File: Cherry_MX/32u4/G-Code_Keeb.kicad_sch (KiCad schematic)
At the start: 45 parts, among them J1 Conn_01x04, SW1 SW_Push_45deg, SW10 SW_Push_45deg, SW11 SW_Push_45deg, SW12 SW_Push_45deg, SW13 SW_Push_45deg, SW14 SW_Push_45deg, SW15 SW_Push_45deg, SW16 SW_Push_45deg, SW17 SW_Push_45deg, SW18 SW_Push_45deg, SW19 SW_Push_45deg, SW2 SW_Push_45deg, SW20 SW_Push_45deg, SW21 SW_Push_45deg, SW22 SW_Push_45deg, SW23 SW_Push_45deg, SW24 SW_Push, SW25 SW_Push, SW3 SW_Push_45deg, SW4 SW_Push_45deg, SW5 SW_Push_45deg, SW6 SW_Push_45deg, SW7 SW_Push_45deg, SW8 SW_Push_45deg, SW9 SW_Push_45deg, U1 ATmega32U4-A, Y1 16MHz

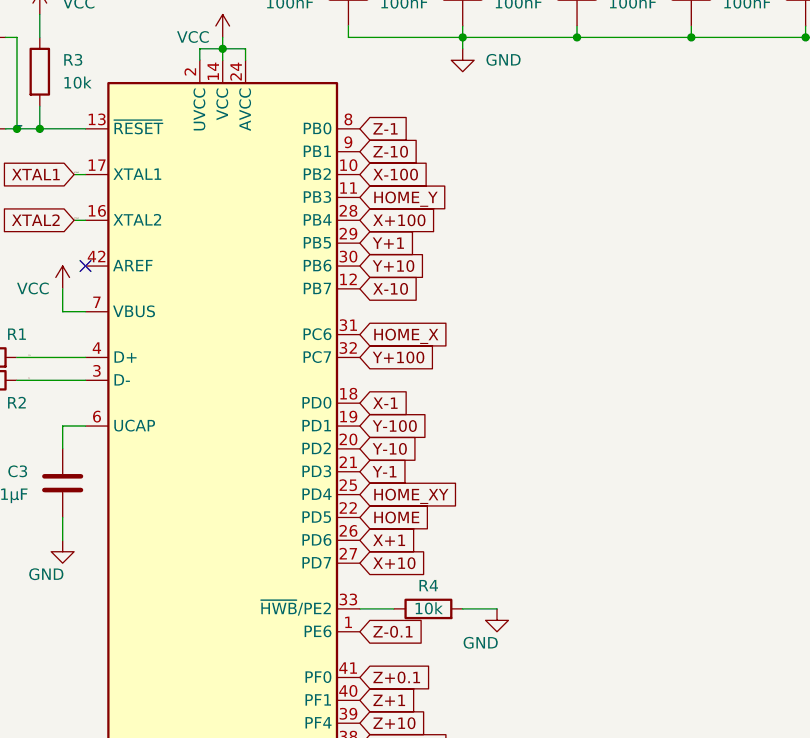
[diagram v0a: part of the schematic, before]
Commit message: Fixed mistake on X axis
The X axis values were mirrored, this commit fix that. That also includes the silkscreen.
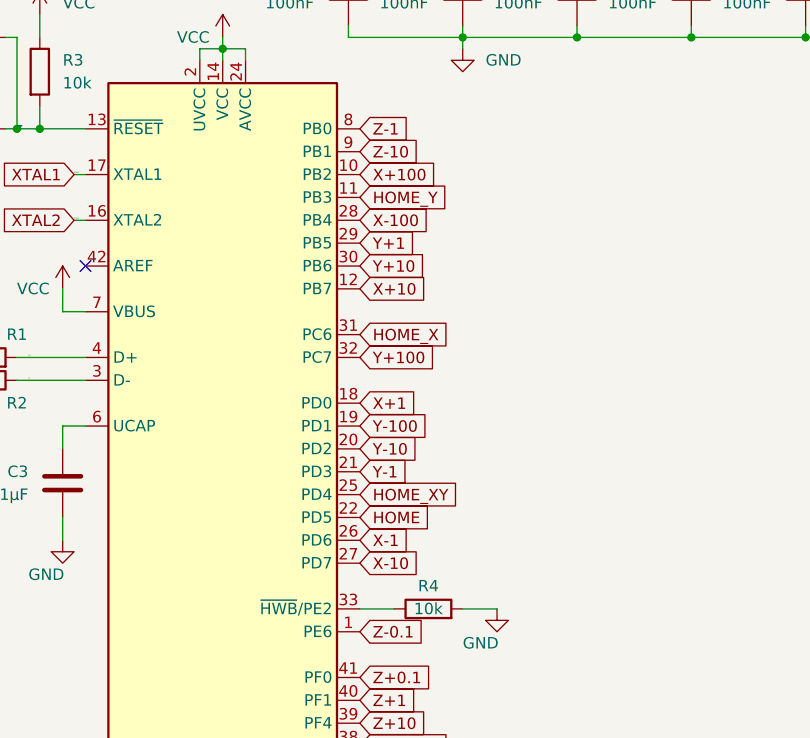
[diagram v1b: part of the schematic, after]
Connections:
- net X+1: now also U1.18 (PD0); no longer U1.26 (PD6)
- net X+10: now also U1.12 (PB7); no longer U1.27 (PD7)
- net X+100: now also U1.10 (PB2); no longer U1.28 (PB4)
- net X-1: now also U1.26 (PD6); no longer U1.18 (PD0)
- net X-10: now also U1.27 (PD7); no longer U1.12 (PB7)
- net X-100: now also U1.28 (PB4); no longer U1.10 (PB2)
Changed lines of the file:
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@@
     )
   )
-  (global_label "X-1" (shape input) (at 218.44 72.39 0) (fields_autoplaced)
-    (effects (font (size 1.27 1.27)) (justify left))
-    (property "Intersheet References" "${INTERSHEET_REFS}" (id 0) (at 224.8445 72.3106 0)
+  (global_label "X-1" (shape input) (at 218.44 87.63 0) (fields_autoplaced)
+    (effects (font (size 1.27 1.27)) (justify left))
+    (property "Intersheet References" "${INTERSHEET_REFS}" (id 0) (at 224.8445 87.5506 0)
       (effects (font (size 1.27 1.27)) (justify left) hide)
     )
@@
     )
   )
-  (global_label "X+10" (shape input) (at 218.44 90.17 0) (fields_autoplaced)
-    (effects (font (size 1.27 1.27)) (justify left))
-    (property "Intersheet References" "${INTERSHEET_REFS}" (id 0) (at 226.0541 90.0906 0)
+  (global_label "X+10" (shape input) (at 218.44 59.69 0) (fields_autoplaced)
+    (effects (font (size 1.27 1.27)) (justify left))
+    (property "Intersheet References" "${INTERSHEET_REFS}" (id 0) (at 226.0541 59.6106 0)
       (effects (font (size 1.27 1.27)) (justify left) hide)
     )
@@
     )
   )
-  (global_label "X+1" (shape input) (at 218.44 87.63 0) (fields_autoplaced)
-    (effects (font (size 1.27 1.27)) (justify left))
-    (property "Intersheet References" "${INTERSHEET_REFS}" (id 0) (at 224.8445 87.5506 0)
+  (global_label "X+1" (shape input) (at 218.44 72.39 0) (fields_autoplaced)
+    (effects (font (size 1.27 1.27)) (justify left))
+    (property "Intersheet References" "${INTERSHEET_REFS}" (id 0) (at 224.8445 72.3106 0)
       (effects (font (size 1.27 1.27)) (justify left) hide)
     )
@@
     )
   )
-  (global_label "X+100" (shape input) (at 218.44 52.07 0) (fields_autoplaced)
+  (global_label "X+100" (shape input) (at 218.44 46.99 0) (fields_autoplaced)
+    (effects (font (size 1.27 1.27)) (justify left))
+    (property "Intersheet References" "${INTERSHEET_REFS}" (id 0) (at 227.2636 46.9106 0)
+      (effects (font (size 1.27 1.27)) (justify left) hide)
+    )
+  )
+  (global_label "Y-1" (shape input) (at 76.2 54.61 90) (fields_autoplaced)
+    (effects (font (size 1.27 1.27)) (justify left))
+    (property "Intersheet References" "${INTERSHEET_REFS}" (id 0) (at 76.1206 48.3264 90)
+      (effects (font (size 1.27 1.27)) (justify left) hide)
+    )
+  )
+  (global_label "XTAL1" (shape input) (at 168.91 46.99 0) (fields_autoplaced)
+    (effects (font (size 1.27 1.27)) (justify left))
+    (property "Intersheet References" "${INTERSHEET_REFS}" (id 0) (at 176.8264 46.9106 0)
+      (effects (font (size 1.27 1.27)) (justify left) hide)
+    )
+  )
+  (global_label "HOME_XY" (shape input) (at 218.44 82.55 0) (fields_autoplaced)
+    (effects (font (size 1.27 1.27)) (justify left))
+    (property "Intersheet References" "${INTERSHEET_REFS}" (id 0) (at 229.3802 82.4706 0)
+      (effects (font (size 1.27 1.27)) (justify left) hide)
+    )
+  )
+  (global_label "X+1" (shape input) (at 66.04 39.37 90) (fields_autoplaced)
+    (effects (font (size 1.27 1.27)) (justify left))
+    (property "Intersheet References" "${INTERSHEET_REFS}" (id 0) (at 65.9606 32.9655 90)
+      (effects (font (size 1.27 1.27)) (justify left) hide)
+    )
+  )
+  (global_label "Z-10" (shape input) (at 96.52 71.12 0) (fields_autoplaced)
+    (effects (font (size 1.27 1.27)) (justify left))
+    (property "Intersheet References" "${INTERSHEET_REFS}" (id 0) (at 104.1341 71.0406 0)
+      (effects (font (size 1.27 1.27)) (justify left) hide)
+    )
+  )
+  (global_label "HOME_XY" (shape input) (at 76.2 85.09 90) (fields_autoplaced)
+    (effects (font (size 1.27 1.27)) (justify left))
+    (property "Intersheet References" "${INTERSHEET_REFS}" (id 0) (at 76.1206 74.1498 90)
+      (effects (font (size 1.27 1.27)) (justify left) hide)
+    )
+  )
+  (global_label "X-100" (shape input) (at 218.44 52.07 0) (fields_autoplaced)
     (effects (font (size 1.27 1.27)) (justify left))
     (property "Intersheet References" "${INTERSHEET_REFS}" (id 0) (at 227.2636 51.9906 0)
@@
     )
   )
-  (global_label "Y-1" (shape input) (at 76.2 54.61 90) (fields_autoplaced)
-    (effects (font (size 1.27 1.27)) (justify left))
-    (property "Intersheet References" "${INTERSHEET_REFS}" (id 0) (at 76.1206 48.3264 90)
-      (effects (font (size 1.27 1.27)) (justify left) hide)
-    )
-  )
-  (global_label "XTAL1" (shape input) (at 168.91 46.99 0) (fields_autoplaced)
-    (effects (font (size 1.27 1.27)) (justify left))
-    (property "Intersheet References" "${INTERSHEET_REFS}" (id 0) (at 176.8264 46.9106 0)
-      (effects (font (size 1.27 1.27)) (justify left) hide)
-    )
-  )
-  (global_label "HOME_XY" (shape input) (at 218.44 82.55 0) (fields_autoplaced)
-    (effects (font (size 1.27 1.27)) (justify left))
-    (property "Intersheet References" "${INTERSHEET_REFS}" (id 0) (at 229.3802 82.4706 0)
-      (effects (font (size 1.27 1.27)) (justify left) hide)
-    )
-  )
-  (global_label "X+1" (shape input) (at 66.04 39.37 90) (fields_autoplaced)
-    (effects (font (size 1.27 1.27)) (justify left))
-    (property "Intersheet References" "${INTERSHEET_REFS}" (id 0) (at 65.9606 32.9655 90)
-      (effects (font (size 1.27 1.27)) (justify left) hide)
-    )
-  )
-  (global_label "Z-10" (shape input) (at 96.52 71.12 0) (fields_autoplaced)
-    (effects (font (size 1.27 1.27)) (justify left))
-    (property "Intersheet References" "${INTERSHEET_REFS}" (id 0) (at 104.1341 71.0406 0)
-      (effects (font (size 1.27 1.27)) (justify left) hide)
-    )
-  )
-  (global_label "HOME_XY" (shape input) (at 76.2 85.09 90) (fields_autoplaced)
-    (effects (font (size 1.27 1.27)) (justify left))
-    (property "Intersheet References" "${INTERSHEET_REFS}" (id 0) (at 76.1206 74.1498 90)
-      (effects (font (size 1.27 1.27)) (justify left) hide)
-    )
-  )
-  (global_label "X-100" (shape input) (at 218.44 46.99 0) (fields_autoplaced)
-    (effects (font (size 1.27 1.27)) (justify left))
-    (property "Intersheet References" "${INTERSHEET_REFS}" (id 0) (at 227.2636 46.9106 0)
-      (effects (font (size 1.27 1.27)) (justify left) hide)
-    )
-  )
   (global_label "HOME_Y" (shape input) (at 66.04 85.09 90) (fields_autoplaced)
     (effects (font (size 1.27 1.27)) (justify left))
@@
     )
   )
-  (global_label "X-10" (shape input) (at 218.44 59.69 0) (fields_autoplaced)
-    (effects (font (size 1.27 1.27)) (justify left))
-    (property "Intersheet References" "${INTERSHEET_REFS}" (id 0) (at 226.0541 59.6106 0)
-      (effects (font (size 1.27 1.27)) (justify left) hide)
-    )
+  (global_label "X-10" (shape input) (at 218.44 90.17 0) (fields_autoplaced)
+    (effects (font (size 1.27 1.27)) (justify left))
+    (property "Intersheet References" "${INTERSHEET_REFS}" (id 0) (at 226.0541 90.0906 0)
+      (effects (font (size 1.27 1.27)) (justify left) hide)
+    )
